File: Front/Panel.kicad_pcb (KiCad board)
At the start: 2 copper layers, 383.5 x 264 mm, 23 parts, among them SW9 RUNSTOP

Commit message: Front
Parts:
- removed +12V: LED +12, RobsFoots:FP-LED_D5.0mm
- removed -12V: LED -12, RobsFoots:FP-LED_D5.0mm
- removed the G*** at (7.62, 136.4)
- removed H1 (x18): MountingHole_Pad, MountingHole:MountingHole_3.2mm_M3_DIN965_Pad
- removed SW9: RUNSTOP, RobsFoots:FP-MINITOGLE
- added G***: LOGO, RobsFoots:TOBINLOGO, F.Cu at (195.2, 88.8)
- added REF**: MountingHole_3.2mm_M3_DIN965_Pad, MountingHole:MountingHole_3.2mm_M3_DIN965_Pad, F.Cu at (210.1, 67.3)
- added REF**: MountingHole_3.2mm_M3_DIN965_Pad, MountingHole:MountingHole_3.2mm_M3_DIN965_Pad, F.Cu at (203.1, 126.3)
- added REF**: MountingHole_3.2mm_M3_DIN965_Pad, MountingHole:MountingHole_3.2mm_M3_DIN965_Pad, F.Cu at (120.8, 128.3)
- added REF**: MountingHole_3.2mm_M3_DIN965_Pad, MountingHole:MountingHole_3.2mm_M3_DIN965_Pad, F.Cu at (120.8, 67.3)
- added REF**: MountingHole_3.2mm_M3_DIN965_Pad, MountingHole:MountingHole_3.2mm_M3_DIN965_Pad, F.Cu at (127.8, 69.3)
- added REF**: MountingHole_3.2mm_M3_DIN965_Pad, MountingHole:MountingHole_3.2mm_M3_DIN965_Pad, F.Cu at (127.8, 126.3)
- added REF**: MountingHole_3.2mm_M3_DIN965_Pad, MountingHole:MountingHole_3.2mm_M3_DIN965_Pad, F.Cu at (203.1, 69.3)
- added REF**: MountingHole_3.2mm_M3_DIN965_Pad, MountingHole:MountingHole_3.2mm_M3_DIN965_Pad, F.Cu at (210.1, 128.3)
- G***: moved to B.Cu
- moved G*** 188.8 mm to (195.3, 86.8), turned to 180 degrees
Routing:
- removed copper zone on B.Cu, net GND
- removed copper zone on F.Cu, net GND
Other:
- board size 383.5 x 264 mm -> 95.3 x 67 mm
- board text added: "100S"
- board text added: "10S"
- board text added: "1S"
- board text added: "CLAYTUNE - ControlMenu V0.1.0 - By TwinTurbo - JLCJLCJLCJLC"
- board text added: "Enter"
- board text removed: "BIG RED BUSS"
- board text removed: "CLAYTUNE"
- board text removed: "CLAYTUNE - Big Red Buss V0.1.0 - By TwinTurbo - JLCJLCJLCJLC"
- board text removed: "For Kate By TwinTurbo"
- board text removed: "OFF"
- board text removed: "ON"

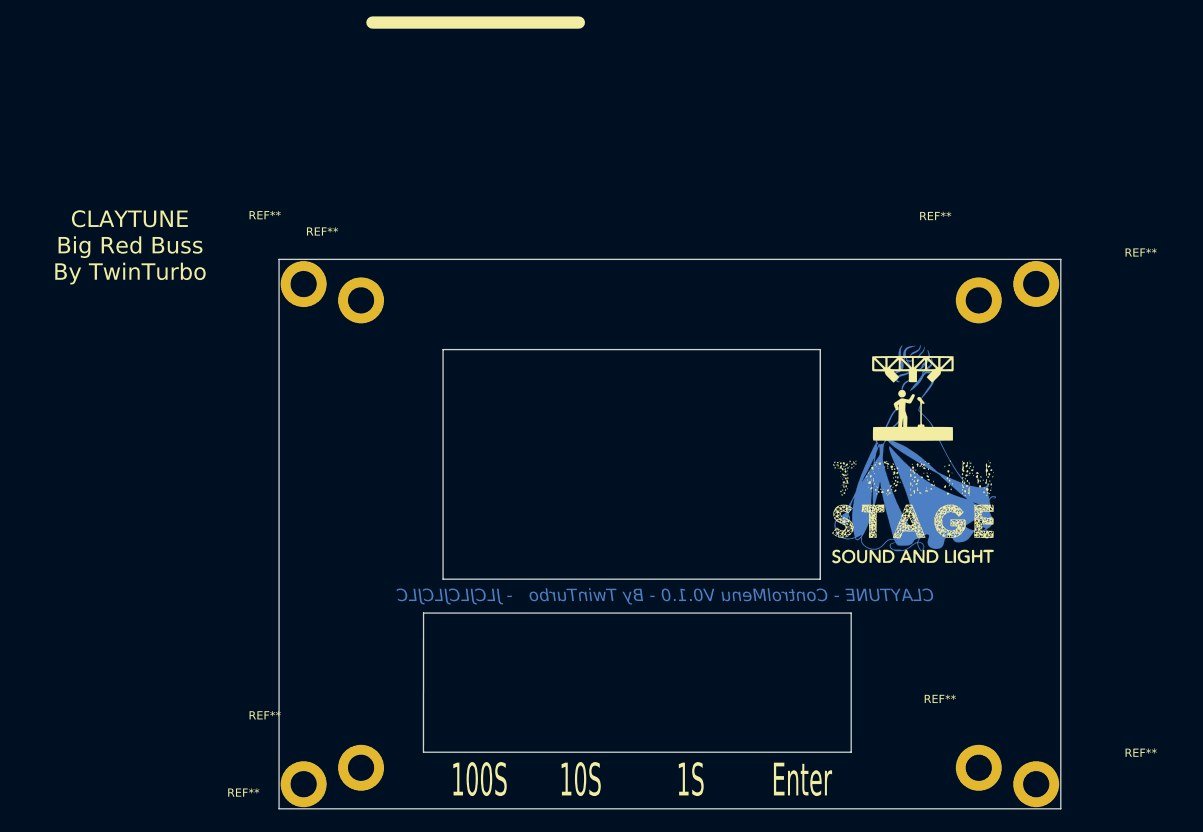
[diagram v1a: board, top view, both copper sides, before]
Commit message: PCB Routed Manualy
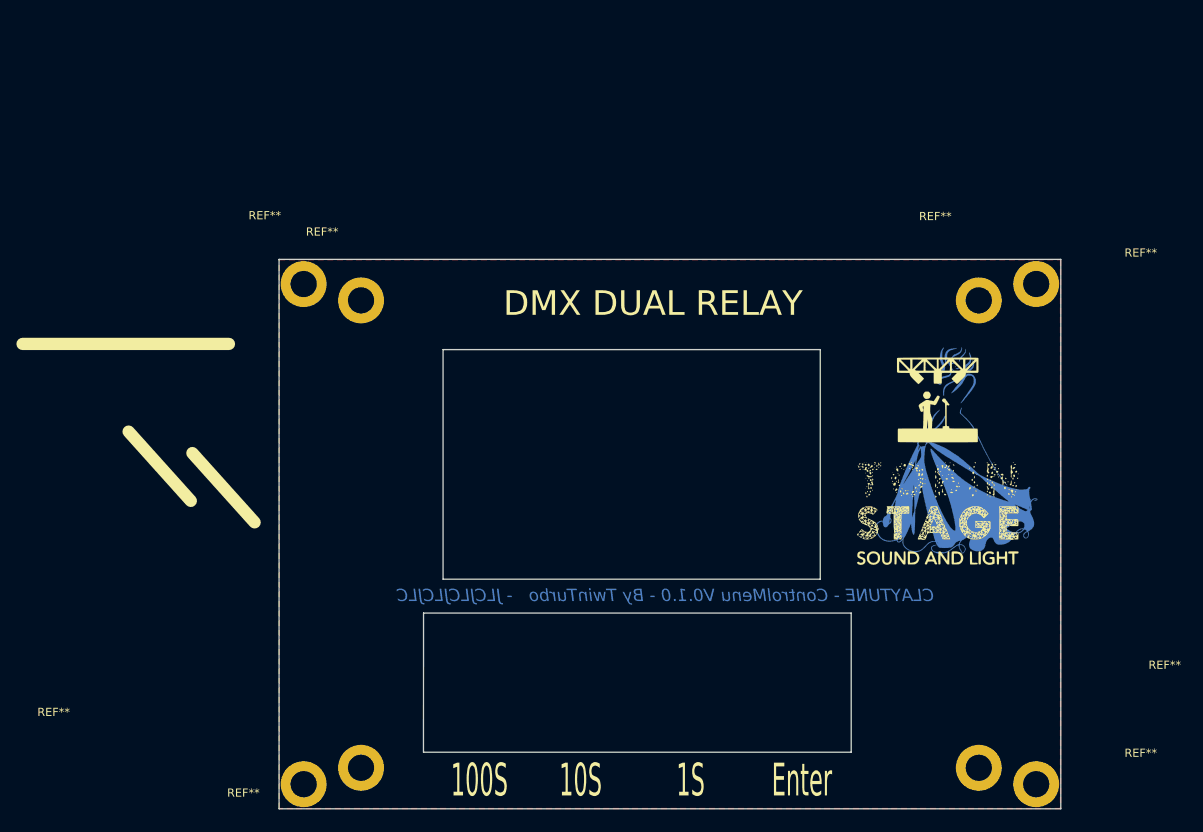
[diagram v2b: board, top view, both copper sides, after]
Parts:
- moved G1 5.06 mm to (200.4, 87.0)
- moved G*** 3.04 mm to (198.2, 89.0)
- renumbered G*** to G1
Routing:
- added copper zone on F.Cu, net GND
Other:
- board text added: "Control PCB"
- board text added: "DMX DUAL RELAY"
- board text removed: "Big Red Buss- PCB V 0.1.0"
- board text removed: "CLAYTUNE Big Red Buss By TwinTurbo"
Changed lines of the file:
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@@
   (general
     (thickness 1.6)
-    (drawings 20)
+    (drawings 22)
     (tracks 0)
     (zones 0)
@@
     (tags "mounting hole 3.2mm m3 din965")
     (attr virtual)
-    (fp_text reference REF** (at -4.74 -8.36) (layer F.SilkS)
+    (fp_text reference REF** (at 22.68 -12.53) (layer F.SilkS)
       (effects (font (size 1 1) (thickness 0.15)))
     )
@@
     (tags "mounting hole 3.2mm m3 din965")
     (attr virtual)
-    (fp_text reference REF** (at -4.74 -8.36) (layer F.SilkS)
+    (fp_text reference REF** (at -30.49 -8.78) (layer F.SilkS)
       (effects (font (size 1 1) (thickness 0.15)))
     )
@@
   )
   (module RobsFoots:TOBINLOGO (layer F.Cu)
-    (at 195.15 88.82)
-    (fp_text reference G*** (at 17.55 2.89) (layer F.SilkS) hide
+    (at 198.18 89.01)
+    (fp_text reference G*** (at 20.66 3.38) (layer F.SilkS) hide
       (effects (font (size 1.524 1.524) (thickness 0.3)))
     )
-    (fp_text value LOGO (at 15.92 0.51) (layer F.SilkS) hide
+    (fp_text value LOGO (at 20.79 0.41) (layer F.SilkS) hide
       (effects (font (size 1.524 1.524) (thickness 0.3)))
     )
@@
   )
   (module ROBSLIBRARY:GFX1FC (layer B.Cu)
-    (at 195.34 86.76 180)
-    (fp_text reference G*** (at -25.43 2.4) (layer B.SilkS) hide
+    (at 200.39 87.04 180)
+    (fp_text reference G1 (at -25.43 2.4) (layer B.SilkS) hide
       (effects (font (size 1.524 1.524) (thickness 0.3)) (justify mirror))
     )
@@
       (xy 1.392042 3.685611) (xy 1.411526 3.663938)) (layer B.Cu) (width 0.01))
   )
+  (gr_line (start 107.22 87.91) (end 114.81 96.36) (layer F.SilkS) (width 1.5))
+  (gr_line (start 86.51 74.6) (end 111.68 74.6) (layer F.SilkS) (width 1.5))
   (gr_line (start 135.4 124.39) (end 135.41 107.42) (layer Edge.Cuts) (width 0.05))
   (gr_line (start 187.56 124.39) (end 135.4 124.39) (layer Edge.Cuts) (width 0.05))
@@
   (gr_line (start 213.12 131.29) (end 213.12 64.29) (layer Edge.Cuts) (width 0.05))
   (gr_line (start 117.79 131.29) (end 117.79 64.29) (layer Edge.Cuts) (width 0.05))
-  (gr_text "Big Red Buss- PCB V 0.1.0" (at 231.42 173.66) (layer Dwgs.User)
+  (gr_text "Control PCB" (at 231.42 173.66) (layer Dwgs.User)
     (effects (font (size 4 4) (thickness 0.15)))
   )
-  (gr_line (start 129.18 35.41) (end 154.35 35.41) (layer F.SilkS) (width 1.5))
-  (gr_text "CLAYTUNE\nBig Red Buss\nBy TwinTurbo\n " (at 99.61 64.24) (layer F.SilkS)
-    (effects (font (size 2 2) (thickness 0.5)))
+  (gr_line (start 99.44 85.29) (end 107.03 93.74) (layer F.SilkS) (width 1.5))
+  (gr_text "DMX DUAL RELAY \n " (at 163.39 72.08) (layer F.SilkS)
+    (effects (font (size 3 3) (thickness 0.5)))
   )
   (gr_text "CLAYTUNE - ControlMenu V0.1.0 - By TwinTurbo   - JLCJLCJLCJLC" (at 164.97 105.26) (layer B.Cu)
     (effects (font (size 1.5 1.5) (thickness 0.3) italic) (justify mirror))
   )
+  (zone (net 1) (net_name GND) (layer F.Cu) (hatch edge 0.508)
+    (connect_pads (clearance 0.508))
+    (min_thickness 0.254)
+    (fill yes (arc_segments 32) (thermal_gap 0.508) (thermal_bridge_width 0.508))
+    (polygon
+      (pts
+        (xy 213.09 131.26) (xy 117.82 131.26) (xy 117.82 64.32) (xy 213.09 64.32)
+      )
+    )
+  )
 )
